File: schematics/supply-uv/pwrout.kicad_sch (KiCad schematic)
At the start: 76 parts, among them Q10 STP13NK60Z, Q11 STP13NK60Z, Q12 IRLML0030, Q7 IRLML0030, Q8 IRLML5203, Q9 IRLML0030, U15 EL817, U16 UC3525, U17 OP213ESZ, U18 IRS21867S, U19 EL817, U20 INA169

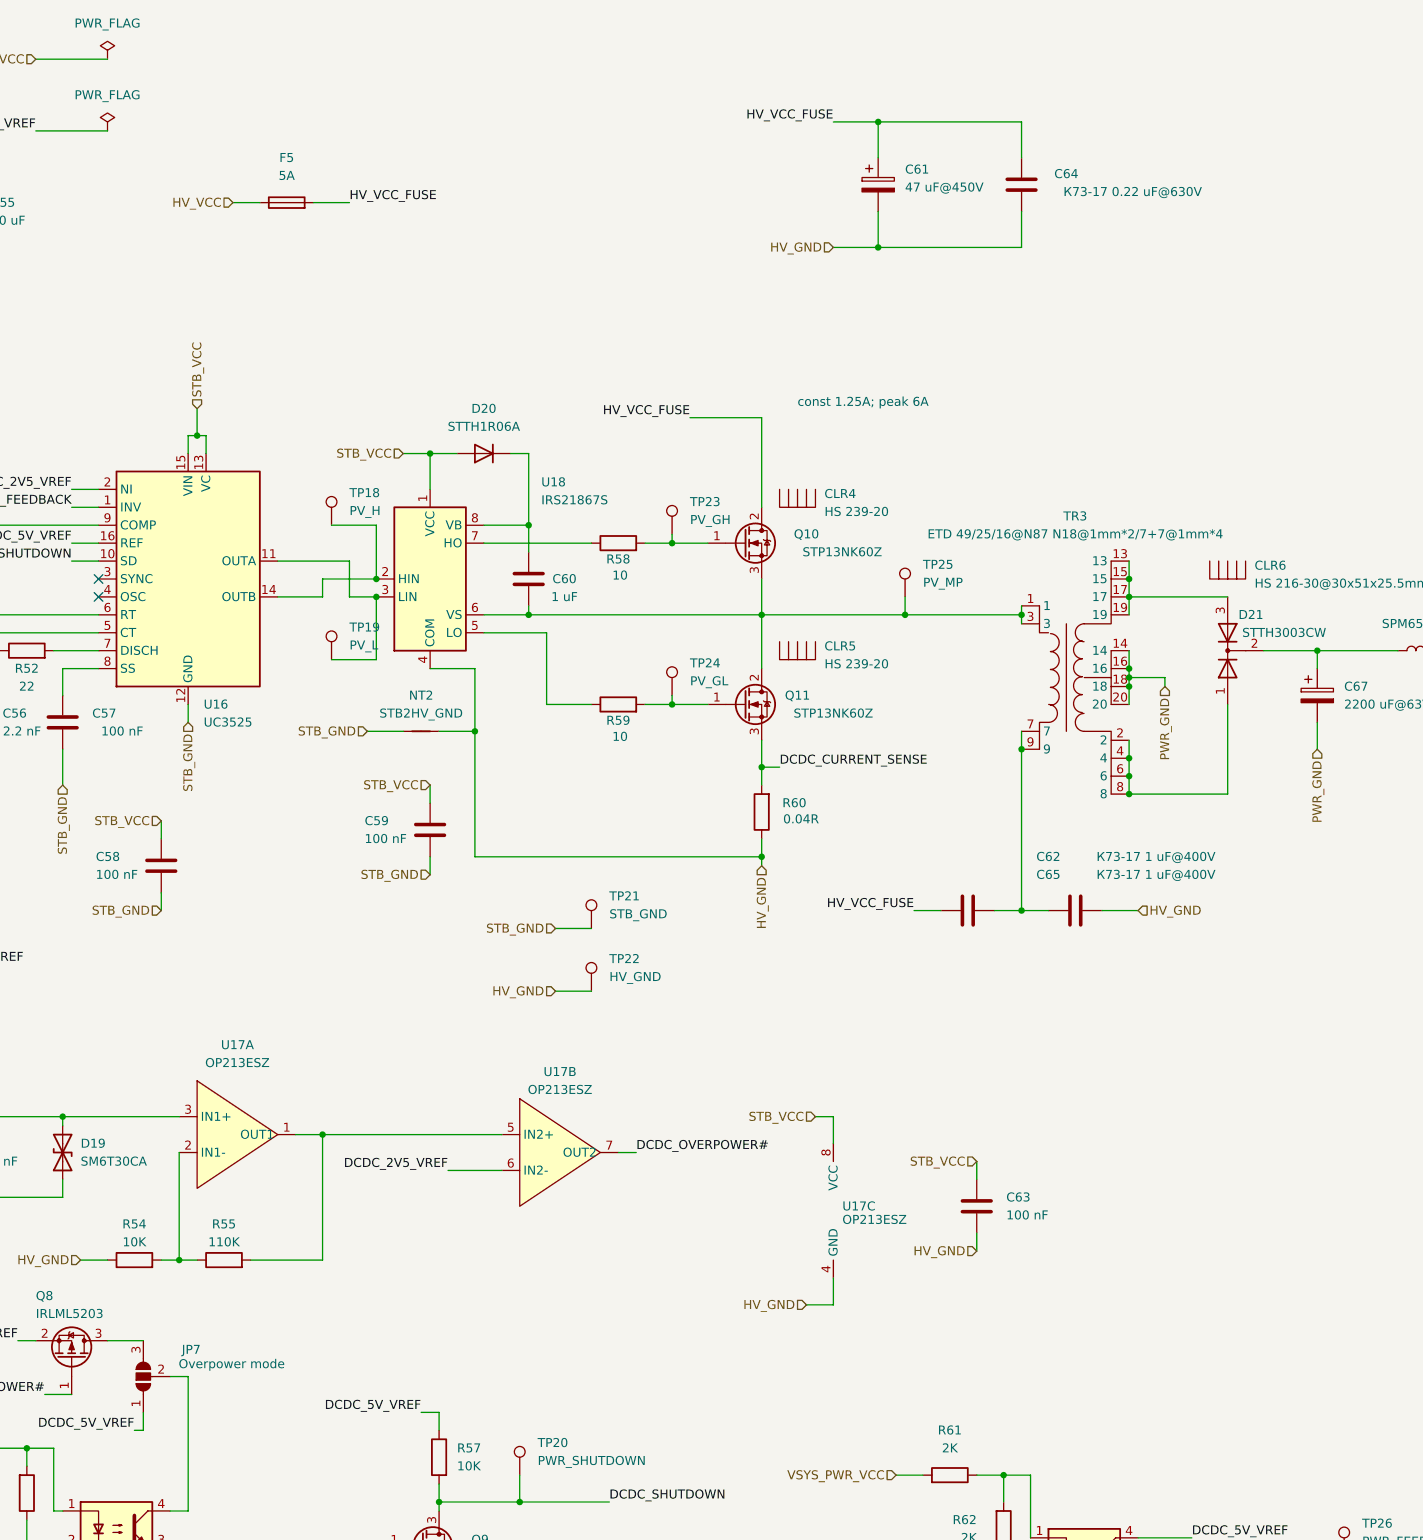
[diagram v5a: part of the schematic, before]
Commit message: some changes in board routing
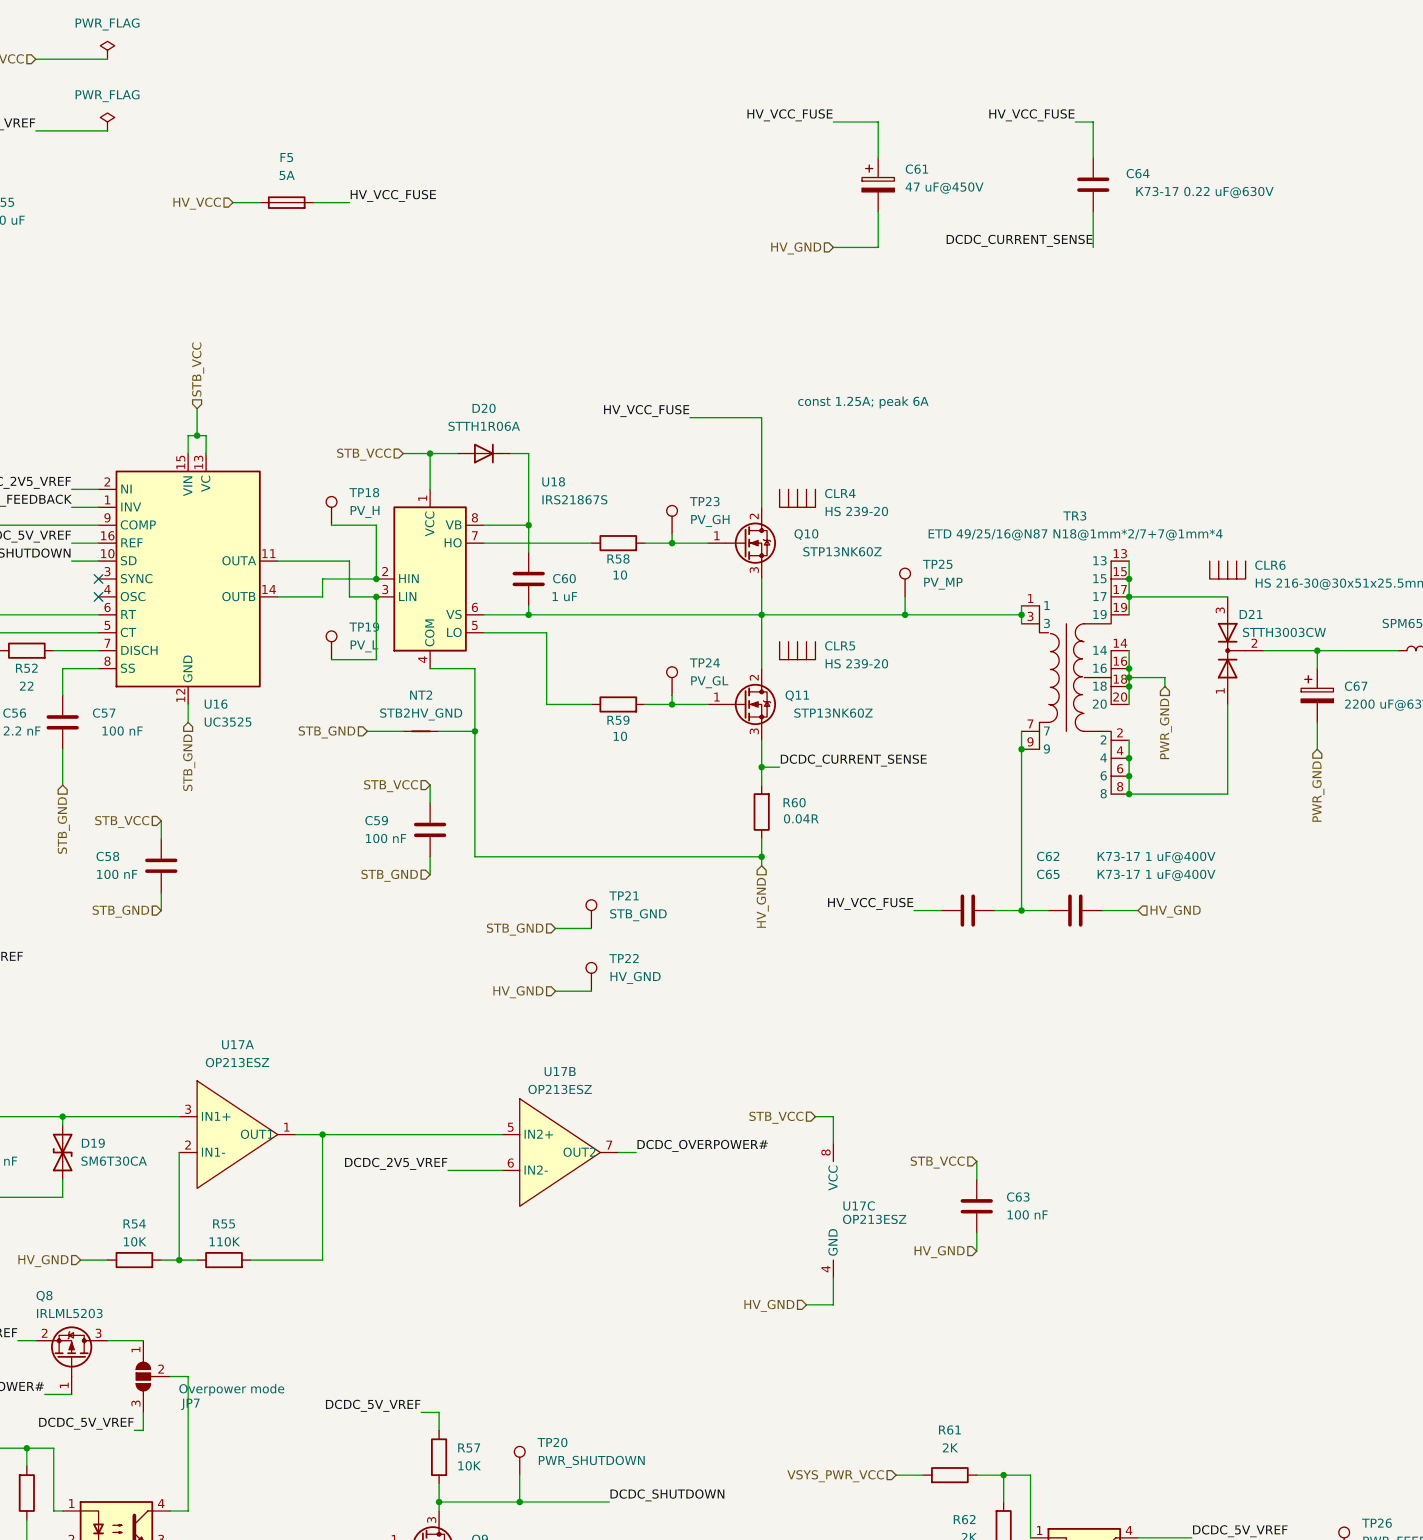
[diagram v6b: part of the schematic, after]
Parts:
- JP7: footprint Connector_PinSocket_2.54mm:PinSocket_1x03_P2.54mm_Vertical -> Jumper:SolderJumper-3_P1.3mm_Bridged2Bar12_RoundedPad1.0x1.5mm_NumberLabels
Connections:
- net DCDC_5V_VREF: now also JP7.3 (B); no longer JP7.1 (A)
- net DCDC_CURRENT_SENSE: now also C64.1
- net HV_GND: no longer C64.1
- net at Q8.3 (D): now also JP7.1 (A); no longer JP7.3 (B)
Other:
- moved on the sheet: C64
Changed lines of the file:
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@@
 	)
 	(junction
-		(at 185.42 48.26)
-		(diameter 0)
-		(color 0 0 0 0)
-	)
-	(junction
 		(at 168.91 134.62)
 		(diameter 0)
@@
 	)
 	(junction
-		(at 185.42 30.48)
-		(diameter 0)
-		(color 0 0 0 0)
-	)
-	(junction
 		(at 106.68 173.99)
 		(diameter 0)
@@
 	(wire
 		(pts
-			(xy 185.42 48.26) (xy 205.74 48.26)
-		)
-		(stroke
-			(width 0)
-			(type default)
-		)
-	)
-	(wire
-		(pts
 			(xy 80.01 215.9) (xy 81.28 215.9)
 		)
@@
 	(wire
 		(pts
-			(xy 205.74 30.48) (xy 185.42 30.48)
-		)
-		(stroke
-			(width 0)
-			(type default)
-		)
-	)
-	(wire
-		(pts
 			(xy 55.88 241.3) (xy 55.88 243.84)
 		)
@@
 	(wire
 		(pts
-			(xy 205.74 35.56) (xy 205.74 30.48)
+			(xy 215.9 35.56) (xy 215.9 30.48)
 		)
 		(stroke
@@
 	(wire
 		(pts
-			(xy 76.2 203.2) (xy 81.28 203.2)
-		)
-		(stroke
-			(width 0)
-			(type default)
-		)
-	)
-	(wire
-		(pts
 			(xy 203.2 222.25) (xy 207.01 222.25)
 		)
@@
 	(wire
 		(pts
+			(xy 81.28 213.36) (xy 81.28 215.9)
+		)
+		(stroke
+			(width 0)
+			(type default)
+		)
+	)
+	(wire
+		(pts
 			(xy 33.02 156.21) (xy 33.02 158.75)
 		)
@@
 	(wire
 		(pts
-			(xy 205.74 43.18) (xy 205.74 48.26)
+			(xy 215.9 43.18) (xy 215.9 48.26)
 		)
 		(stroke
@@
 	(wire
 		(pts
+			(xy 76.2 203.2) (xy 81.28 203.2)
+		)
+		(stroke
+			(width 0)
+			(type default)
+		)
+	)
+	(wire
+		(pts
 			(xy 382.27 146.05) (xy 382.27 148.59)
 		)
@@
 	(wire
 		(pts
+			(xy 213.36 30.48) (xy 215.9 30.48)
+		)
+		(stroke
+			(width 0)
+			(type default)
+		)
+	)
+	(wire
+		(pts
 			(xy 152.4 90.17) (xy 156.21 90.17)
 		)
@@
 	(wire
 		(pts
-			(xy 81.28 213.36) (xy 81.28 215.9)
-		)
-		(stroke
-			(width 0)
-			(type default)
-		)
-	)
-	(wire
-		(pts
 			(xy 57.15 102.87) (xy 74.93 102.87)
 		)
@@
 		)
 	)
+	(label "HV_VCC_FUSE"
+		(at 213.36 30.48 180)
+		(fields_autoplaced yes)
+		(effects
+			(font
+				(size 1.27 1.27)
+			)
+			(justify right bottom)
+		)
+	)
 	(label "DCDC_2V5_VREF"
 		(at 49.53 149.86 0)
@@
 		)
 	)
+	(label "DCDC_CURRENT_SENSE"
+		(at 215.9 48.26 180)
+		(fields_autoplaced yes)
+		(effects
+			(font
+				(size 1.27 1.27)
+			)
+			(justify right bottom)
+		)
+	)
 	(label "DCDC_FEEDBACK"
 		(at 71.12 85.09 180)
@@
 		(lib_id "Jumper:SolderJumper_3_Open")
 		(at 81.28 208.28 90)
+		(mirror x)
 		(unit 1)
 		(exclude_from_sim yes)
@@
 		(dnp no)
 		(property "Reference" "JP7"
-			(at 89.408 204.47 90)
+			(at 89.408 212.09 90)
 			(effects
 				(font
@@
 		)
 		(property "Value" "Overpower mode"
-			(at 101.346 206.502 90)
+			(at 101.346 210.058 90)
 			(effects
 				(font
@@
 			)
 		)
-		(property "Footprint" "Connector_PinSocket_2.54mm:PinSocket_1x03_P2.54mm_Vertical"
+		(property "Footprint" "Jumper:SolderJumper-3_P1.3mm_Bridged2Bar12_RoundedPad1.0x1.5mm_NumberLabels"
 			(at 81.28 208.28 0)
 			(effects
@@
 	(symbol
 		(lib_id "Device:C")
-		(at 205.74 39.37 180)
+		(at 215.9 39.37 180)
 		(unit 1)
 		(exclude_from_sim no)
@@
 		(dnp no)
 		(property "Reference" "C64"
-			(at 212.09 37.846 0)
+			(at 222.25 37.846 0)
 			(effects
 				(font
@@
 		)
 		(property "Value" "К73-17 0.22 uF@630V"
-			(at 221.488 40.386 0)
+			(at 231.648 40.386 0)
 			(effects
 				(font
@@
 		)
 		(property "Footprint" "Capacitor_THT:C_Axial_L12.0mm_D6.5mm_P20.00mm_Horizontal"
-			(at 204.7748 35.56 0)
+			(at 214.9348 35.56 0)
 			(effects
 				(font
@@
 		)
 		(property "Datasheet" "~"
-			(at 205.74 39.37 0)
+			(at 215.9 39.37 0)
 			(effects
 				(font
@@
 		)
 		(property "Description" "Unpolarized capacitor"
-			(at 205.74 39.37 0)
+			(at 215.9 39.37 0)
 			(effects
 				(font

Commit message: Boards prepared to order
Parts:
- renumbered C51 to C52, C52 to C53, C53 to C54, C54 to C55, C55 to C56, C56 to C57, C57 to C58, C58 to C59, C59 to C60, C60 to C61, C61 to C62, C62 to C63, C63 to C64, C64 to C66, C66 to C67, C67 to C68, C68 to C69, C69 to C70, C70 to C71, C71 to C72, TP18 to TP20, TP19 to TP21, TP20 to TP22, TP21 to TP23, TP22 to TP24, TP23 to TP25, TP24 to TP26, TP25 to TP27, TP26 to TP28
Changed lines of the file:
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@@
 		(dnp no)
 		(fields_autoplaced yes)
-		(property "Reference" "TP26"
+		(property "Reference" "TP28"
 			(at 254 229.1079 0)
 			(effects
@@
 			(project "supply-uv"
 				(path "/ef40850c-d0bf-4cba-961b-9aba418f8e73/3be77773-a110-4db5-84df-23304730890a"
-					(reference "TP26")
+					(reference "TP28")
 					(unit 1)
 				)
@@
 		(on_board yes)
 		(dnp no)
-		(property "Reference" "C56"
+		(property "Reference" "C57"
 			(at 64.77 114.3 0)
 			(effects
@@
 			(project "supply-uv"
 				(path "/ef40850c-d0bf-4cba-961b-9aba418f8e73/3be77773-a110-4db5-84df-23304730890a"
-					(reference "C56")
+					(reference "C57")
 					(unit 1)
 				)
@@
 		(on_board yes)
 		(dnp no)
-		(property "Reference" "C68"
+		(property "Reference" "C69"
 			(at 274.32 110.49 0)
 			(effects
@@
 			(project "supply-uv"
 				(path "/ef40850c-d0bf-4cba-961b-9aba418f8e73/3be77773-a110-4db5-84df-23304730890a"
-					(reference "C68")
+					(reference "C69")
 					(unit 1)
 				)
@@
 		(dnp no)
 		(fields_autoplaced yes)
-		(property "Reference" "TP21"
+		(property "Reference" "TP23"
 			(at 147.32 140.2079 0)
 			(effects
@@
 			(project "supply-uv"
 				(path "/ef40850c-d0bf-4cba-961b-9aba418f8e73/3be77773-a110-4db5-84df-23304730890a"
-					(reference "TP21")
+					(reference "TP23")
 					(unit 1)
 				)
@@
 		(dnp no)
 		(fields_autoplaced yes)
-		(property "Reference" "TP25"
+		(property "Reference" "TP27"
 			(at 191.77 93.2179 0)
 			(effects
@@
 			(project "supply-uv"
 				(path "/ef40850c-d0bf-4cba-961b-9aba418f8e73/3be77773-a110-4db5-84df-23304730890a"
-					(reference "TP25")
+					(reference "TP27")
 					(unit 1)
 				)
@@
 		(dnp no)
 		(fields_autoplaced yes)
-		(property "Reference" "TP23"
+		(property "Reference" "TP25"
 			(at 158.75 84.3279 0)
 			(effects
@@
 			(project "supply-uv"
 				(path "/ef40850c-d0bf-4cba-961b-9aba418f8e73/3be77773-a110-4db5-84df-23304730890a"
-					(reference "TP23")
+					(reference "TP25")
 					(unit 1)
 				)
@@
 		(on_board yes)
 		(dnp no)
-		(property "Reference" "C64"
+		(property "Reference" "C66"
 			(at 222.25 37.846 0)
 			(effects
@@
 			(project "supply-uv"
 				(path "/ef40850c-d0bf-4cba-961b-9aba418f8e73/3be77773-a110-4db5-84df-23304730890a"
-					(reference "C64")
+					(reference "C66")
 					(unit 1)
 				)
@@
 		(dnp no)
 		(fields_autoplaced yes)
-		(property "Reference" "TP24"
+		(property "Reference" "TP26"
 			(at 158.75 107.1879 0)
 			(effects
@@
 			(project "supply-uv"
 				(path "/ef40850c-d0bf-4cba-961b-9aba418f8e73/3be77773-a110-4db5-84df-23304730890a"
-					(reference "TP24")
+					(reference "TP26")
 					(unit 1)
 				)
@@
 		(on_board yes)
 		(dnp no)
-		(property "Reference" "C62"
+		(property "Reference" "C63"
 			(at 209.55 134.62 90)
 			(effects
@@
 			(project "supply-uv"
 				(path "/ef40850c-d0bf-4cba-961b-9aba418f8e73/3be77773-a110-4db5-84df-23304730890a"
-					(reference "C62")
+					(reference "C63")
 					(unit 1)
 				)
@@
 		(on_board yes)
 		(dnp no)
-		(property "Reference" "C63"
+		(property "Reference" "C64"
 			(at 207.01 182.88 0)
 			(effects
@@
 			(project "supply-uv"
 				(path "/ef40850c-d0bf-4cba-961b-9aba418f8e73/3be77773-a110-4db5-84df-23304730890a"
-					(reference "C63")
+					(reference "C64")
 					(unit 1)
 				)
@@
 		(on_board yes)
 		(dnp no)
-		(property "Reference" "C51"
+		(property "Reference" "C52"
 			(at 35.56 92.71 0)
 			(effects
@@
 			(project "supply-uv"
 				(path "/ef40850c-d0bf-4cba-961b-9aba418f8e73/3be77773-a110-4db5-84df-23304730890a"
-					(reference "C51")
+					(reference "C52")
 					(unit 1)
 				)
@@
 		(dnp no)
 		(fields_autoplaced yes)
-		(property "Reference" "TP19"
+		(property "Reference" "TP21"
 			(at 110.49 102.1079 0)
 			(effects
@@
 			(project "supply-uv"
 				(path "/ef40850c-d0bf-4cba-961b-9aba418f8e73/3be77773-a110-4db5-84df-23304730890a"
-					(reference "TP19")
+					(reference "TP21")
 					(unit 1)
 				)
@@
 		(on_board yes)
 		(dnp no)
-		(property "Reference" "C57"
+		(property "Reference" "C58"
 			(at 77.47 114.3 0)
 			(effects
@@
 			(project "supply-uv"
 				(path "/ef40850c-d0bf-4cba-961b-9aba418f8e73/3be77773-a110-4db5-84df-23304730890a"
-					(reference "C57")
+					(reference "C58")
 					(unit 1)
 				)
@@
 		(on_board yes)
 		(dnp no)
-		(property "Reference" "C69"
+		(property "Reference" "C70"
 			(at 308.61 137.16 0)
 			(effects
@@
 			(project "supply-uv"
 				(path "/ef40850c-d0bf-4cba-961b-9aba418f8e73/3be77773-a110-4db5-84df-23304730890a"
-					(reference "C69")
+					(reference "C70")
 					(unit 1)
 				)
@@
 		(on_board yes)
 		(dnp no)
-		(property "Reference" "C67"
+		(property "Reference" "C68"
 			(at 251.46 110.49 0)
 			(effects
@@
 			(project "supply-uv"
 				(path "/ef40850c-d0bf-4cba-961b-9aba418f8e73/3be77773-a110-4db5-84df-23304730890a"
-					(reference "C67")
+					(reference "C68")
 					(unit 1)
 				)
@@
 		(on_board yes)
 		(dnp no)
-		(property "Reference" "C70"
+		(property "Reference" "C71"
 			(at 360.68 135.89 0)
 			(effects
@@
 			(project "supply-uv"
 				(path "/ef40850c-d0bf-4cba-961b-9aba418f8e73/3be77773-a110-4db5-84df-23304730890a"
-					(reference "C70")
+					(reference "C71")
 					(unit 1)
 				)
@@
 		(on_board yes)
 		(dnp no)
-		(property "Reference" "C71"
+		(property "Reference" "C72"
 			(at 386.08 151.13 0)
 			(effects
@@
 			(project "supply-uv"
 				(path "/ef40850c-d0bf-4cba-961b-9aba418f8e73/3be77773-a110-4db5-84df-23304730890a"
-					(reference "C71")
+					(reference "C72")
 					(unit 1)
 				)
@@
 		(on_board yes)
 		(dnp no)
-		(property "Reference" "C66"
+		(property "Reference" "C67"
 			(at 251.46 240.03 0)
 			(effects
@@
 			(project "supply-uv"
 				(path "/ef40850c-d0bf-4cba-961b-9aba418f8e73/3be77773-a110-4db5-84df-23304730890a"
-					(reference "C66")
+					(reference "C67")
 					(unit 1)
 				)
@@
 		(on_board yes)
 		(dnp no)
-		(property "Reference" "C59"
+		(property "Reference" "C60"
 			(at 116.078 129.54 0)
 			(effects
@@
 			(project "supply-uv"
 				(path "/ef40850c-d0bf-4cba-961b-9aba418f8e73/3be77773-a110-4db5-84df-23304730890a"
-					(reference "C59")
+					(reference "C60")
 					(unit 1)
 				)
@@
 		(on_board yes)
 		(dnp no)
-		(property "Reference" "C60"
+		(property "Reference" "C61"
 			(at 140.97 95.25 0)
 			(effects
@@
 			(project "supply-uv"
 				(path "/ef40850c-d0bf-4cba-961b-9aba418f8e73/3be77773-a110-4db5-84df-23304730890a"
-					(reference "C60")
+					(reference "C61")
 					(unit 1)
 				)
@@
 		(dnp no)
 		(fields_autoplaced yes)
-		(property "Reference" "TP18"
+		(property "Reference" "TP20"
 			(at 110.49 83.0579 0)
 			(effects
@@
 			(project "supply-uv"
 				(path "/ef40850c-d0bf-4cba-961b-9aba418f8e73/3be77773-a110-4db5-84df-23304730890a"
-					(reference "TP18")
+					(reference "TP20")
 					(unit 1)
 				)
@@
 		(on_board yes)
 		(dnp no)
-		(property "Reference" "C58"
+		(property "Reference" "C59"
 			(at 77.978 134.62 0)
 			(effects
@@
 			(project "supply-uv"
 				(path "/ef40850c-d0bf-4cba-961b-9aba418f8e73/3be77773-a110-4db5-84df-23304730890a"
-					(reference "C58")
+					(reference "C59")
 					(unit 1)
 				)
@@
 		(dnp no)
 		(fields_autoplaced yes)
-		(property "Reference" "TP22"
+		(property "Reference" "TP24"
 			(at 147.32 149.0979 0)
 			(effects
@@
 			(project "supply-uv"
 				(path "/ef40850c-d0bf-4cba-961b-9aba418f8e73/3be77773-a110-4db5-84df-23304730890a"
-					(reference "TP22")
+					(reference "TP24")
 					(unit 1)
 				)
@@
 		(dnp no)
 		(fields_autoplaced yes)
-		(property "Reference" "TP20"
+		(property "Reference" "TP22"
 			(at 137.16 217.6779 0)
 			(effects
@@
 			(project "supply-uv"
 				(path "/ef40850c-d0bf-4cba-961b-9aba418f8e73/3be77773-a110-4db5-84df-23304730890a"
-					(reference "TP20")
+					(reference "TP22")
 					(unit 1)
 				)
@@
 		(on_board yes)
 		(dnp no)
-		(property "Reference" "C53"
+		(property "Reference" "C54"
 			(at 40.64 151.13 0)
 			(effects
@@
 			(project "supply-uv"
 				(path "/ef40850c-d0bf-4cba-961b-9aba418f8e73/3be77773-a110-4db5-84df-23304730890a"
-					(reference "C53")
+					(reference "C54")
 					(unit 1)
 				)
@@
 		(dnp no)
 		(fields_autoplaced yes)
-		(property "Reference" "C55"
+		(property "Reference" "C56"
 			(at 59.69 41.9099 0)
 			(effects
@@
 			(project "supply-uv"
 				(path "/ef40850c-d0bf-4cba-961b-9aba418f8e73/3be77773-a110-4db5-84df-23304730890a"
-					(reference "C55")
+					(reference "C56")
 					(unit 1)
 				)
@@
 		(dnp no)
 		(fields_autoplaced yes)
-		(property "Reference" "C61"
+		(property "Reference" "C62"
 			(at 189.23 37.2109 0)
 			(effects
@@
 			(project "supply-uv"
 				(path "/ef40850c-d0bf-4cba-961b-9aba418f8e73/3be77773-a110-4db5-84df-23304730890a"
-					(reference "C61")
+					(reference "C62")
 					(unit 1)
 				)
@@
 		(on_board yes)
 		(dnp no)
-		(property "Reference" "C52"
+		(property "Reference" "C53"
 			(at 36.322 42.672 0)
 			(effects
@@
 			(project "supply-uv"
 				(path "/ef40850c-d0bf-4cba-961b-9aba418f8e73/3be77773-a110-4db5-84df-23304730890a"
-					(reference "C52")
+					(reference "C53")
 					(unit 1)
 				)
@@
 		(on_board yes)
 		(dnp no)
-		(property "Reference" "C54"
+		(property "Reference" "C55"
 			(at 60.96 175.26 0)
 			(effects
@@
 			(project "supply-uv"
 				(path "/ef40850c-d0bf-4cba-961b-9aba418f8e73/3be77773-a110-4db5-84df-23304730890a"
-					(reference "C54")
+					(reference "C55")
 					(unit 1)
 				)
